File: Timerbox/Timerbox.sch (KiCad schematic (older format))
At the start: 40 parts, among them CON1 AVR-ISP-6, IC1 ATTINY4313-P, K1 ROT, P1 CON, P2 BTN1, P3 BTN01, P4 RST, P5 BTN0, Q1 2N3904, U1 78L05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

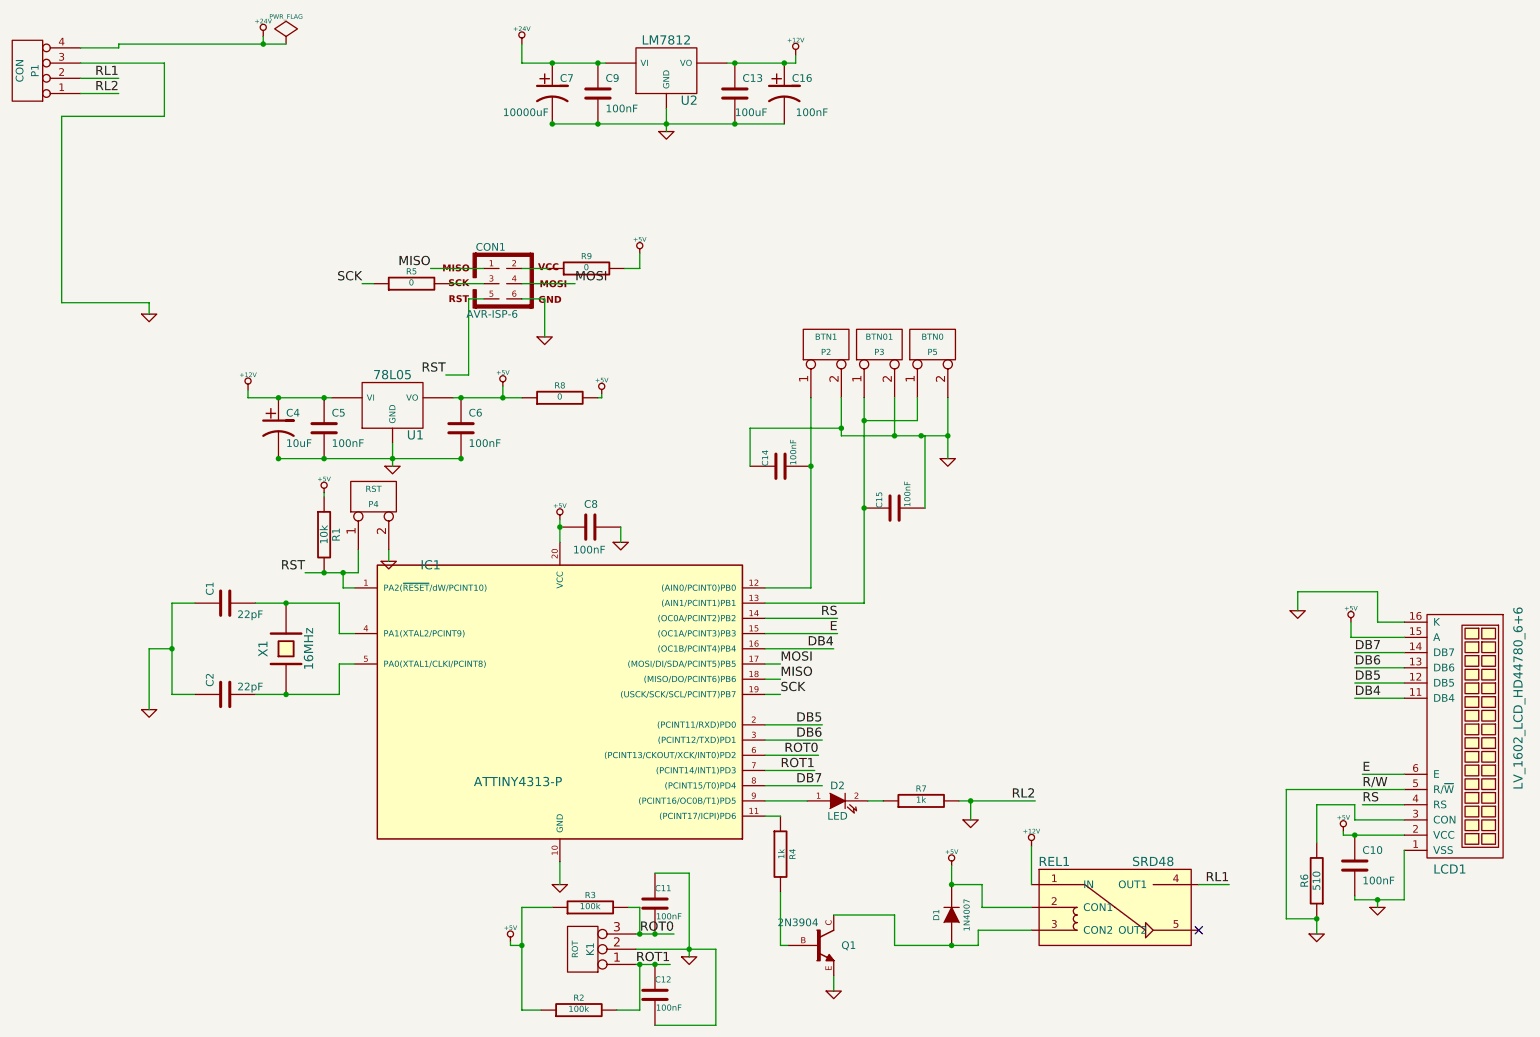
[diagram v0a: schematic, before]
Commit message: Added some libs and some new circuits
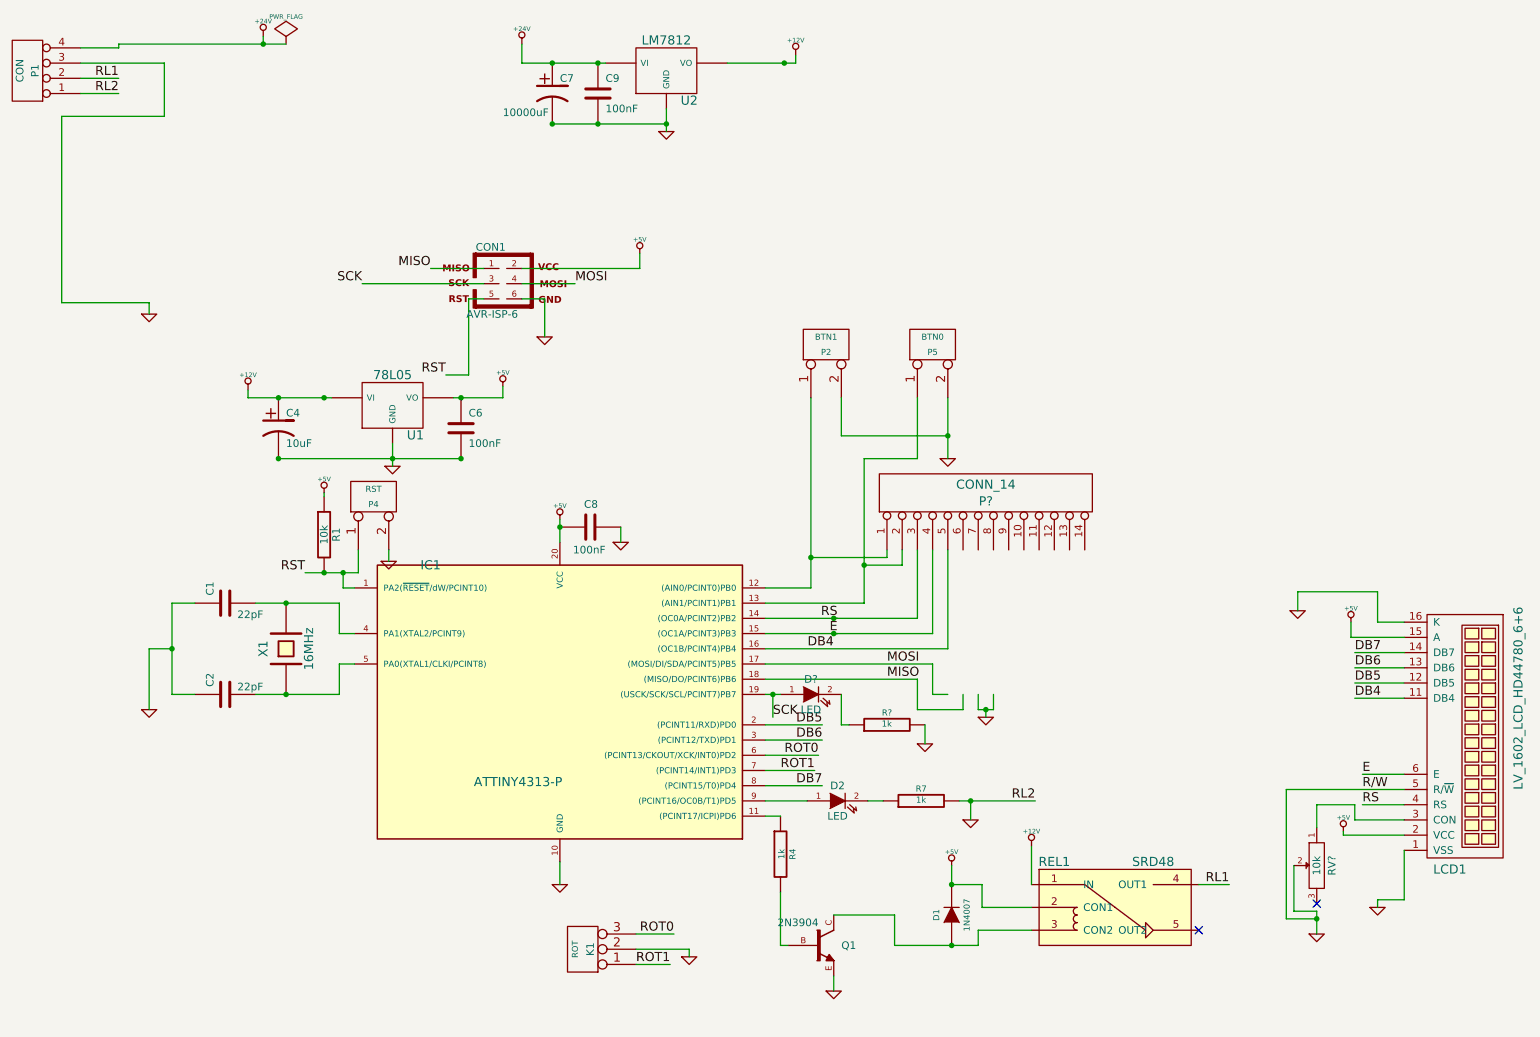
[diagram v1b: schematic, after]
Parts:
- removed C10, C13, C5: 100nF, symbol C
- removed C11, C12, C14, C15: 100nF, ~, symbol C
- removed C16: 100uF, symbol CP1
- removed P3: BTN01, symbol CONN_2
- removed R2, R3: 100k, ~, symbol R
- removed R5, R8, R9: 0, ~, symbol R
- removed R6: 510, symbol R
- added D?: LED, ~, symbol LED
- added P?: CONN_14, symbol CONN_14
- added R?: 1k, ~, symbol R
- added RV?: 10k, ~, symbol POT
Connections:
- net +5V: now also CON1.2
- net DB4: now also P?.5 (P5)
- net E: now also P?.4 (P4)
- net GND: now also R?.2, RV?.2
- net RS: now also P?.3 (P3)
- net SCK: now also CON1.3, D?.1 (A)
- net at IC1.12 ((AIN0/PCINT0)PB0), P2.1 (P1): now also P?.1 (P1)
- net at IC1.13 ((AIN1/PCINT1)PB1), P5.1 (P1): now also P?.2 (P2)
- net at LCD1.3 (CON): now also RV?.1
- new net: D?.2 (K), R?.1
- no-connect marks 1 -> 2
